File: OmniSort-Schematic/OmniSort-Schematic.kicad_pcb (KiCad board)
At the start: 2 copper layers, 90 x 93 mm, 28 parts, among them J1 Conn_01x04, SW1 SW_Push, SW2 SW_Push, SW3 SW_Push, SW4 SW_Push, SW5 SW_Push, SW6 SW_Push, SW7 SW_Push, SW8 SW_Push, SW9 RotaryEncoder_Switch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

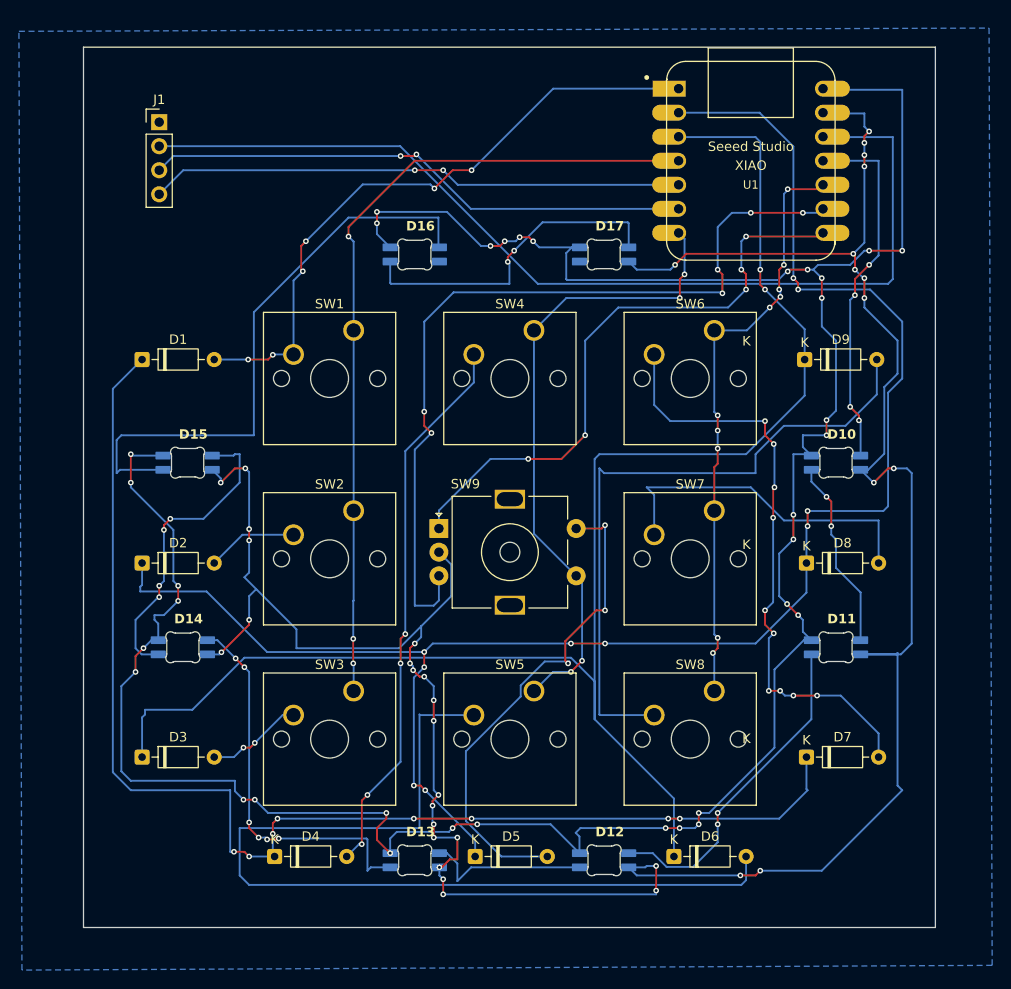
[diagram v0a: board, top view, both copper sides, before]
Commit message: Upload Partially Completed 3D Case models
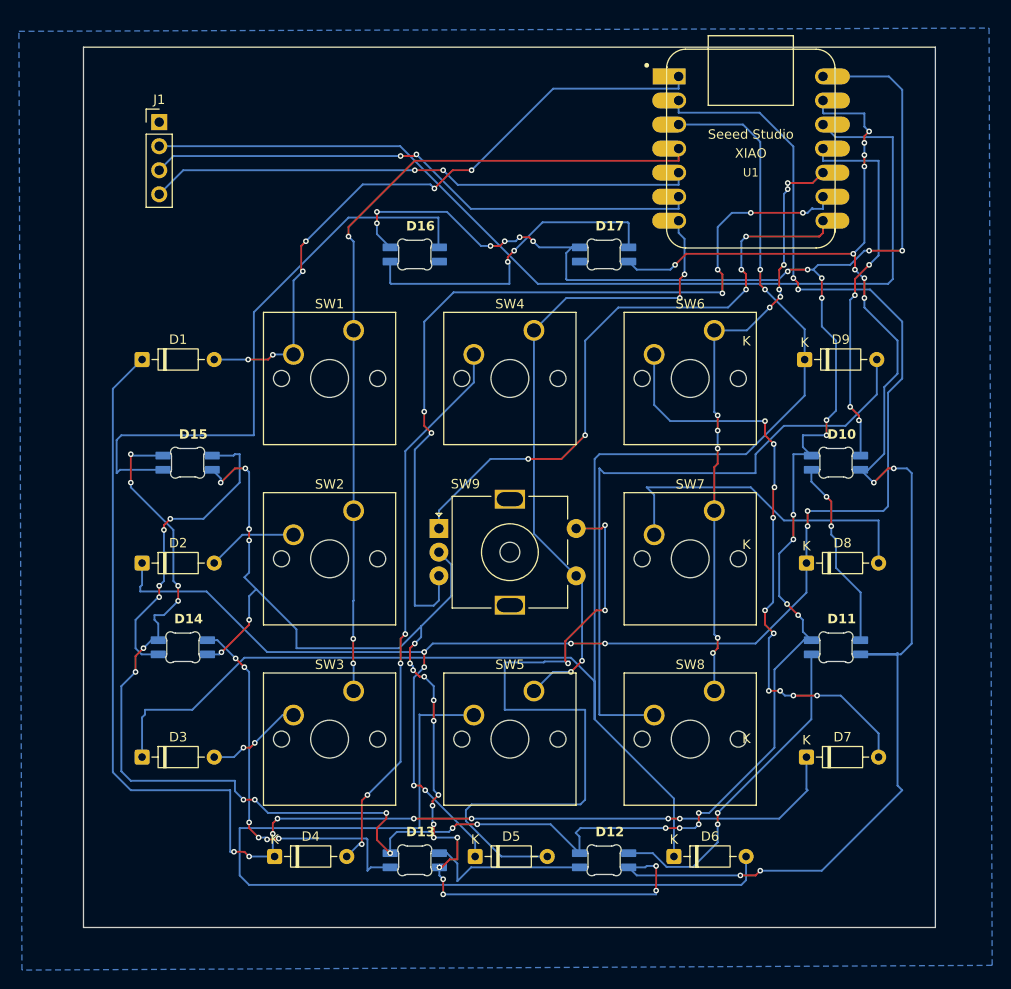
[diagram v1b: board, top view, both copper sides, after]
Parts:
- moved U1 1.29 mm to (165.5, 32.7)
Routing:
- net Net-(D5-A): track 53.5 -> 74.7 mm
- net /ENC_B: track 88.4 -> 89.7 mm
- net GND: track 277.6 -> 278.9 mm
- net /ROW1: track 182.7 -> 184.0 mm
- net /COL1: track 67.6 -> 68.9 mm
- net /OLED_SDA: track 56.6 -> 57.9 mm
- net /OLED_SCL: track 58.0 -> 59.2 mm
- net /LED_DATA: track 38.7 -> 40.0 mm
- net /ROW0: track 67.7 -> 68.9 mm
- net /ENC_A: track 64.2 -> 65.5 mm
- net /COL0: track 87.1 -> 88.3 mm
- net /COL2: track 63.1 -> 64.0 mm, vias 10 -> 11
- net +5V: track 286.0 -> 286.5 mm
- net +3V3: track 106.1 -> 106.7 mm
- net /ROW2: track 168.0 -> 168.5 mm
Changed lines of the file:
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@@
 	(footprint "footprints:XIAO-Generic-Hybrid-14P-2.54-21X17.8MM"
 		(layer "F.Cu")
-		(at 165.5 34)
+		(at 165.5 32.712015)
 		(property "Reference" "U1"
 			(at 0 2.54 0)
@@
 	)
 	(segment
+		(start 181.5 26.5)
+		(end 180.092015 25.092015)
+		(width 0.2)
+		(layer "B.Cu")
+		(net "+5V")
+	)
+	(segment
 		(start 173.5 63)
 		(end 171 63)
@@
 	)
 	(segment
-		(start 173.245 26.5)
-		(end 173.125 26.38)
-		(width 0.2)
-		(layer "B.Cu")
-		(net "+5V")
-	)
-	(segment
 		(start 99 98.5)
 		(end 100 99.5)
@@
 	)
 	(segment
+		(start 180.092015 25.092015)
+		(end 173.125 25.092015)
+		(width 0.2)
+		(layer "B.Cu")
+		(net "+5V")
+	)
+	(segment
 		(start 105 80.5)
 		(end 103.5 82)
@@
 	)
 	(segment
-		(start 181.5 26.5)
-		(end 173.245 26.5)
-		(width 0.2)
-		(layer "B.Cu")
-		(net "+5V")
-	)
-	(segment
 		(start 146.1 46.6)
 		(end 168.4 46.6)
@@
 	)
 	(segment
+		(start 173.125 28.92)
+		(end 173.125 27.632015)
+		(width 0.2)
+		(layer "B.Cu")
+		(net "GND")
+	)
+	(segment
 		(start 133 111.5)
 		(end 155.5 111.5)
@@
 	)
 	(segment
-		(start 169.4 37)
-		(end 172.665 37)
+		(start 172.026951 36.350064)
+		(end 173.125 35.252015)
 		(width 0.2)
 		(layer "F.Cu")
@@
 	)
 	(segment
-		(start 172.665 37)
-		(end 173.125 36.54)
-		(width 0.2)
-		(layer "F.Cu")
-		(net "/COL2")
-	)
-	(segment
 		(start 162 66)
 		(end 161.64 66.36)
@@
 	)
 	(segment
+		(start 169.4 36.350064)
+		(end 172.026951 36.350064)
+		(width 0.2)
+		(layer "F.Cu")
+		(net "/COL2")
+	)
+	(segment
 		(start 161.64 66.36)
 		(end 161.64 70.97)
@@
 	)
 	(via
+		(at 169.4 36.350064)
+		(size 0.6)
+		(drill 0.3)
+		(layers "F.Cu" "B.Cu")
+		(net "/COL2")
+	)
+	(via
 		(at 162 62.5)
 		(size 0.6)
@@
 	)
 	(segment
+		(start 169.4 37)
+		(end 169.4 36.350064)
+		(width 0.2)
+		(layer "B.Cu")
+		(net "/COL2")
+	)
+	(segment
 		(start 169 45)
 		(end 169 37.5)
@@
 	)
 	(segment
-		(start 166.5 45.5)
-		(end 166.5 32)
-		(width 0.2)
-		(layer "B.Cu")
-		(net "/ROW2")
-	)
-	(segment
-		(start 166.5 32)
-		(end 166 31.5)
-		(width 0.2)
-		(layer "B.Cu")
-		(net "/ROW2")
-	)
-	(segment
 		(start 101.19 92.81)
 		(end 101.19 97)
@@
 	)
 	(segment
-		(start 166 31.5)
-		(end 157.915 31.5)
+		(start 166.5 32)
+		(end 164.672015 30.172015)
+		(width 0.2)
+		(layer "B.Cu")
+		(net "/ROW2")
+	)
+	(segment
+		(start 166.5 45.5)
+		(end 166.5 32)
 		(width 0.2)
 		(layer "B.Cu")
@@
 	)
 	(segment
+		(start 164.672015 30.172015)
+		(end 157.875 30.172015)
+		(width 0.2)
+		(layer "B.Cu")
+		(net "/ROW2")
+	)
+	(segment
 		(start 157.38 101.38)
 		(end 157.38 107.5)
@@
 	)
 	(segment
-		(start 157.915 31.5)
-		(end 157.875 31.46)
-		(width 0.2)
-		(layer "B.Cu")
-		(net "/ROW2")
-	)
-	(segment
 		(start 171.19 58.81)
 		(end 165 65)
@@
 	)
 	(segment
+		(start 157.875 40.332015)
+		(end 157.875 41.62)
+		(width 0.2)
+		(layer "B.Cu")
+		(net "/COL1")
+	)
+	(segment
 		(start 147.05 77.85)
 		(end 147.674265 78.474265)
@@
 	)
 	(segment
+		(start 157.875 28.92)
+		(end 157.875 27.632015)
+		(width 0.2)
+		(layer "B.Cu")
+		(net "/ROW1")
+	)
+	(segment
 		(start 136.38 105.78)
 		(end 136.38 107.5)
@@
 	)
 	(segment
+		(start 157.875 26.38)
+		(end 157.875 25.092015)
+		(width 0.2)
+		(layer "B.Cu")
+		(net "/ROW0")
+	)
+	(segment
 		(start 144.62 26.38)
 		(end 157.875 26.38)
@@
 	)
 	(segment
+		(start 157.875 34)
+		(end 157.875 32.712015)
+		(width 0.2)
+		(layer "F.Cu")
+		(net "/COL0")
+	)
+	(segment
 		(start 130 34)
 		(end 157.875 34)
@@
 	)
 	(segment
+		(start 157.875 36.54)
+		(end 157.875 35.252015)
+		(width 0.2)
+		(layer "B.Cu")
+		(net "/OLED_SDA")
+	)
+	(segment
 		(start 105.54 35)
 		(end 130 35)
@@
 	)
 	(segment
+		(start 157.875 39.08)
+		(end 157.875 37.792015)
+		(width 0.2)
+		(layer "B.Cu")
+		(net "/OLED_SCL")
+	)
+	(segment
 		(start 104.5 33.5)
 		(end 128.5 33.5)
@@
 	)
 	(segment
+		(start 173.125 41.62)
+		(end 173.125 40.332015)
+		(width 0.2)
+		(layer "F.Cu")
+		(net "/ENC_A")
+	)
+	(segment
 		(start 165 42)
 		(end 172.745 42)
@@
 	)
 	(segment
+		(start 171 39.5)
+		(end 171.5 39.5)
+		(width 0.2)
+		(layer "B.Cu")
+		(net "/ENC_B")
+	)
+	(segment
+		(start 173.125 39.08)
+		(end 173.125 37.792015)
+		(width 0.2)
+		(layer "B.Cu")
+		(net "/ENC_B")
+	)
+	(segment
 		(start 132 81)
 		(end 130 81)
@@
 	)
 	(segment
+		(start 171.5 39.5)
+		(end 172 39)
+		(width 0.2)
+		(layer "B.Cu")
+		(net "/ENC_B")
+	)
+	(segment
 		(start 134.1 47.9)
 		(end 162.4 47.9)
@@
 	)
 	(segment
+		(start 172.08 39.08)
+		(end 173.125 39.08)
+		(width 0.2)
+		(layer "B.Cu")
+		(net "/ENC_B")
+	)
+	(segment
 		(start 131 51)
 		(end 134.1 47.9)
@@
 	)
 	(segment
-		(start 171 39.5)
-		(end 172.705 39.5)
-		(width 0.2)
-		(layer "B.Cu")
-		(net "/ENC_B")
-	)
-	(segment
 		(start 131 60.5)
 		(end 131 51)
@@
 	)
 	(segment
-		(start 172.705 39.5)
-		(end 173.125 39.08)
+		(start 172 39)
+		(end 172.08 39.08)
 		(width 0.2)
 		(layer "B.Cu")
@@
 	)
 	(segment
+		(start 173.125 34)
+		(end 173.125 32.712015)
+		(width 0.2)
+		(layer "B.Cu")
+		(net "/LED_DATA")
+	)
+	(segment
 		(start 176 60)
 		(end 176 48.7)
@@
 	)
 	(segment
-		(start 173.165 31.5)
-		(end 173.125 31.46)
+		(start 174.452985 31.5)
+		(end 173.125 30.172015)
 		(width 0.2)
 		(layer "B.Cu")
@@
 	(segment
 		(start 180.5 31.5)
-		(end 173.165 31.5)
+		(end 174.452985 31.5)
 		(width 0.2)
 		(layer "B.Cu")
@@
 	)
 	(segment
-		(start 139.151471 107.5)
-		(end 135.4 103.748529)
+		(start 139.5 92)
+		(end 139.5 87)
 		(width 0.2)
 		(layer "B.Cu")
@@
 	)
 	(segment
-		(start 144 107.5)
-		(end 139.151471 107.5)
+		(start 135.4 102.6)
+		(end 136 102)
 		(width 0.2)
 		(layer "B.Cu")
@@
 	)
 	(segment
-		(start 141.19 89.440101)
-		(end 143.730101 86.9)
+		(start 148 101.5)
+		(end 148 92)
 		(width 0.2)
 		(layer "B.Cu")
@@
 	)
 	(segment
-		(start 141.19 90.599899)
-		(end 141.19 89.440101)
+		(start 139.5 87)
+		(end 143.630101 87)
 		(width 0.2)
 		(layer "B.Cu")
@@
 	)
 	(segment
-		(start 135.4 103.748529)
-		(end 135.4 96.389899)
+		(start 144 107.5)
+		(end 139.151471 107.5)
+		(width 0.2)
+		(layer "B.Cu")
+		(net "Net-(D5-A)")
+	)
+	(segment
+		(start 139.151471 107.5)
+		(end 135.4 103.748529)
+		(width 0.2)
+		(layer "B.Cu")
+		(net "Net-(D5-A)")
+	)
+	(segment
+		(start 147.5 102)
+		(end 148 101.5)
 		(width 0.2)
 		(layer "B.Cu")
@@
 	)
 	(segment
+		(start 143.630101 87)
+		(end 143.730101 86.9)
+		(width 0.2)
+		(layer "B.Cu")
+		(net "Net-(D5-A)")
+	)
+	(segment
+		(start 136 102)
+		(end 147.5 102)
+		(width 0.2)
+		(layer "B.Cu")
+		(net "Net-(D5-A)")
+	)
+	(segment
 		(start 146.334314 86.9)
 		(end 146.334314 86.958578)
@@
 	)
 	(segment
-		(start 135.4 96.389899)
-		(end 141.19 90.599899)
+		(start 148 92)
+		(end 139.5 92)
+		(width 0.2)
+		(layer "B.Cu")
+		(net "Net-(D5-A)")
+	)
+	(segment
+		(start 135.4 103.748529)
+		(end 135.4 102.6)
 		(width 0.2)
 		(layer "B.Cu")

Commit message: Schematic & PCB update
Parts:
- added REF**: MountingHole_4mm, MountingHole:MountingHole_4mm, F.Cu at (180.0, 110.0)
- added REF**: MountingHole_4mm, MountingHole:MountingHole_4mm, F.Cu at (112.5, 41.5)
- added REF**: MountingHole_4mm, MountingHole:MountingHole_4mm, F.Cu at (98.0, 25.0)
- added REF**: MountingHole_4mm, MountingHole:MountingHole_4mm, F.Cu at (102.5, 107.5)
- added REF**: MountingHole_4mm, MountingHole:MountingHole_4mm, F.Cu at (182.0, 25.0)
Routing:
- net +5V: track 286.5 -> 285.1 mm
- net /COL2: track 64.0 -> 63.9 mm, vias 11 -> 10

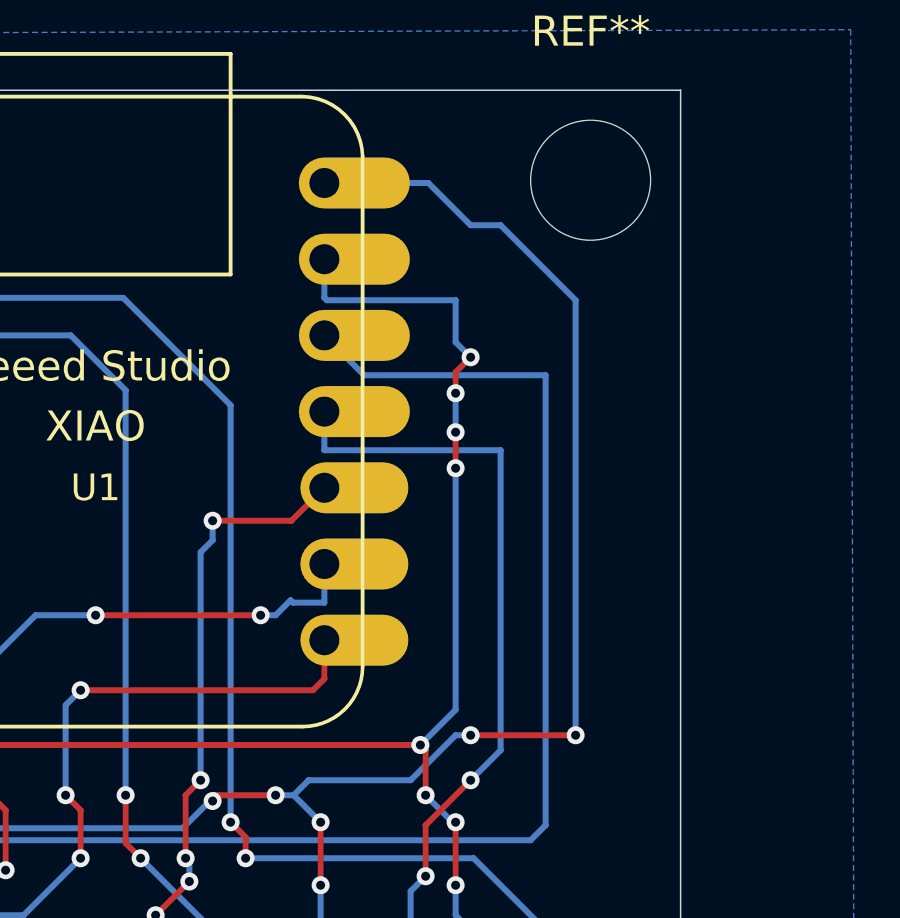
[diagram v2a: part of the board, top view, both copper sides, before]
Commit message: PCB refinement
Adjusted mounting hole sizes and trace routing around the holes
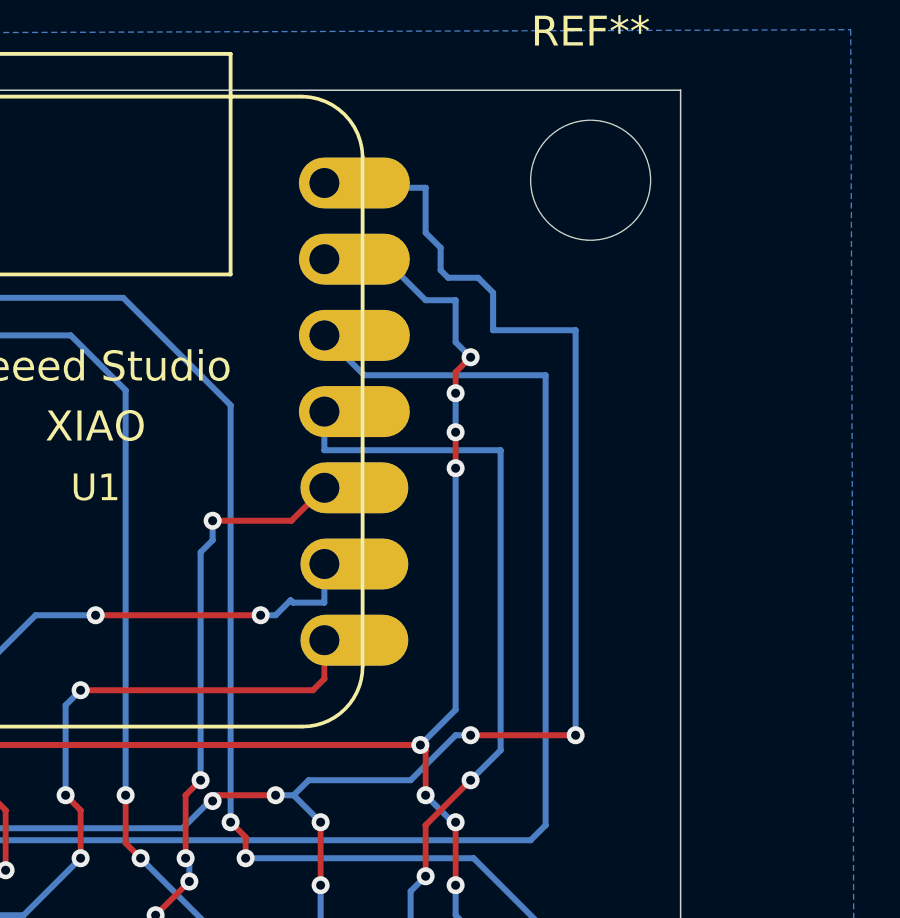
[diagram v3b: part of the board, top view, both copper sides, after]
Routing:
- net +5V: track 285.1 -> 286.5 mm
- net GND: track 278.9 -> 278.2 mm
